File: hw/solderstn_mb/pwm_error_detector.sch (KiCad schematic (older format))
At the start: 14 parts, among them Q1601 DMG1013T, U1601 NE556d, U1602 74LVC1G175dck, U1603 74LVC1G11dck

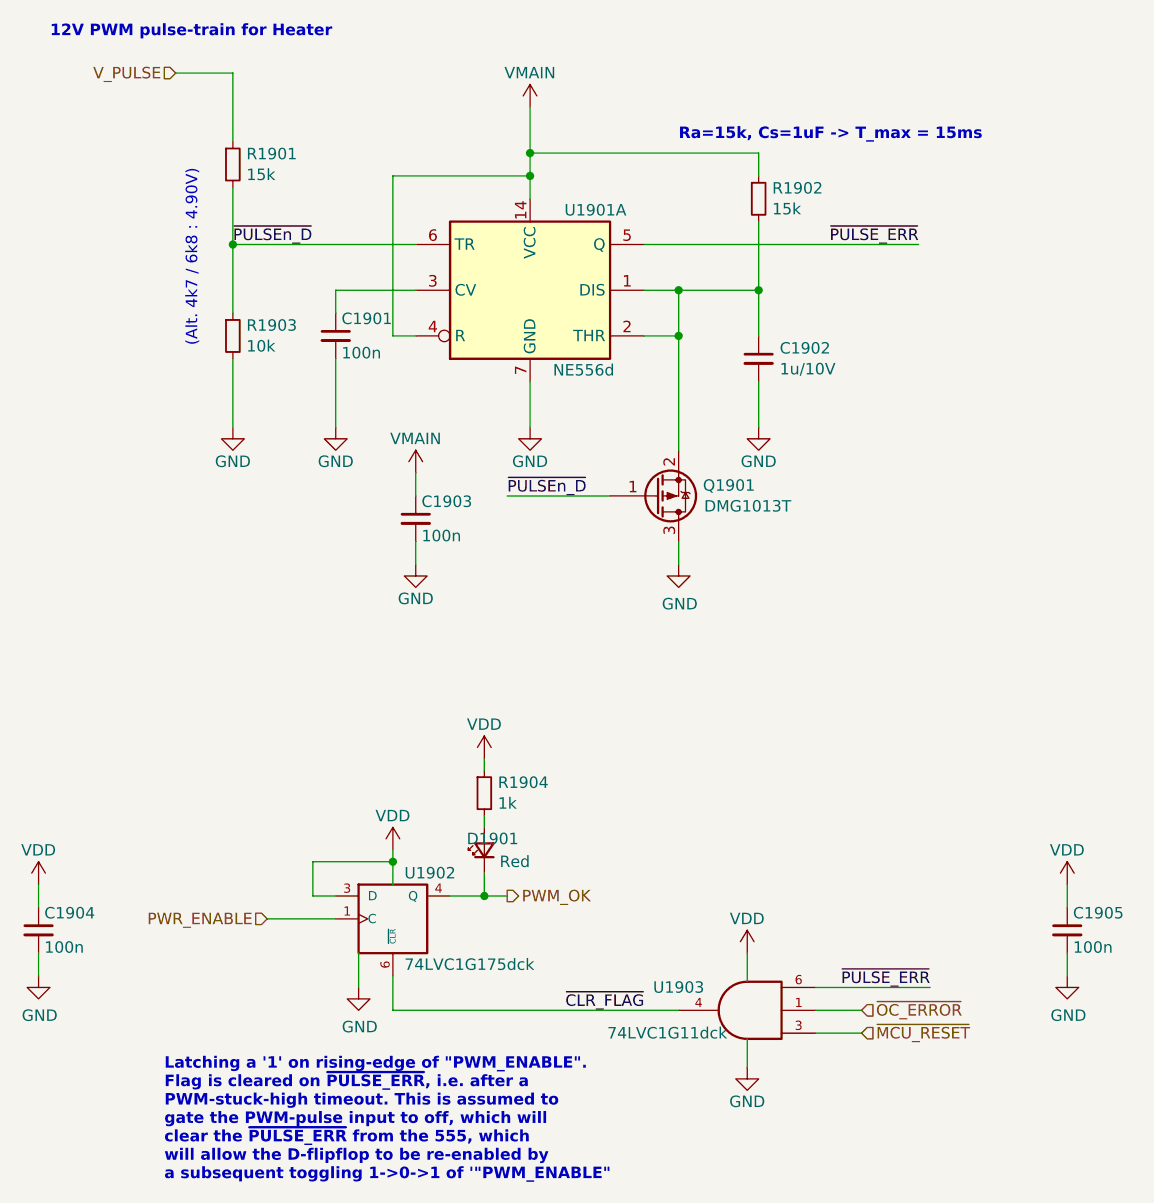
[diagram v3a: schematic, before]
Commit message: Pinout changes to add DS3231 RTC module instead of 32kHz LSE xtal (still keep SMD pads as placeholders). Minor ERC fixes. All footprints specified
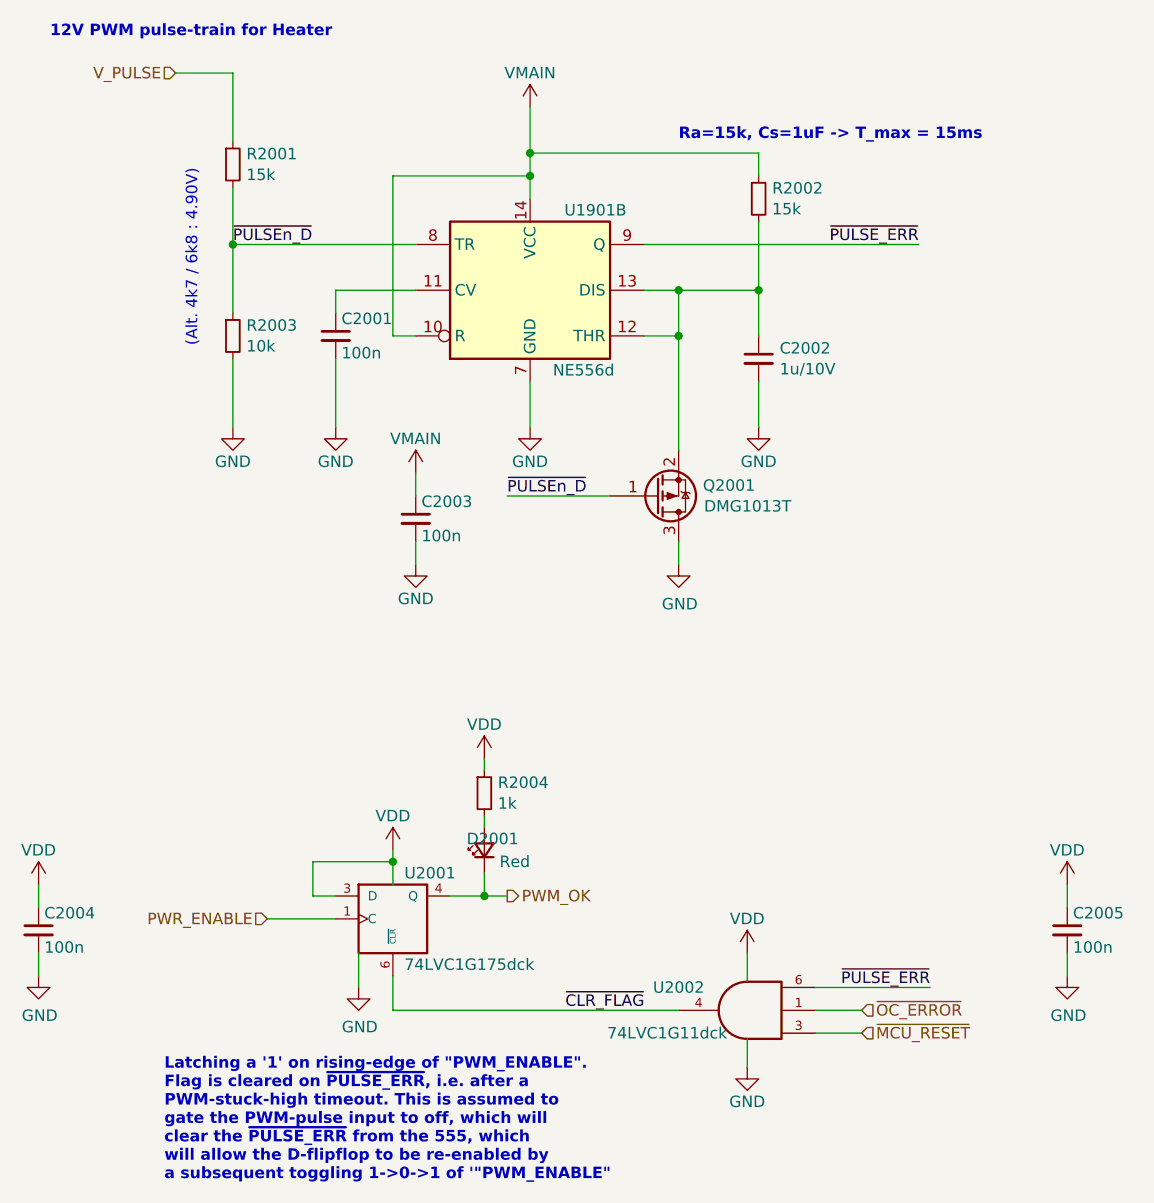
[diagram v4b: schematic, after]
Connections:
- net VMAIN: now also U1601.10 (R); no longer U1601.4 (R)
- net ~PULSE_ERR~: now also U1601.9 (Q); no longer U1601.5 (Q)
- net ~PULSEn_D~: now also U1601.8 (TR); no longer U1601.6 (TR)
- net at C1602.1, Q1601.2 (S), R1602.2: now also U1601.12 (THR), U1601.13 (DIS); no longer U1601.1 (DIS), U1601.2 (THR)
- net at C1601.1: now also U1601.11 (CV); no longer U1601.3 (CV)
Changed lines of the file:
@@
 $Comp
 L Timer:NE556 U1601
-U 1 1 5F5A84E5
+U 2 1 5F5A84E5
 P 4400 2800
 AR Path="/5F785D6E/5F788693/5F5A79BB/5F5A84E5" Ref="U1601"  Part="1"
@@
 F 2 "Package_SO:SOIC-14_3.9x8.7mm_P1.27mm" H 4400 2800 50  0001 C CNN
 F 3 "http://www.ti.com/lit/ds/symlink/ne556.pdf" H 4400 2800 50  0001 C CNN
-	1    4400 2800
+	2    4400 2800
 	1    0    0    -1
 $EndComp
@@
 AR Path="/5F785D6E/5F788A8E/5F5A79BB/5F5A959F" Ref="#PWR01901"  Part="1"
 AR Path="/5F785D6E/5F788A8E/5F5A8042/5F5A959F" Ref="#PWR02001"  Part="1"
-F 0 "#PWR01901" H 4400 1850 50  0001 C CNN
+F 0 "#PWR02001" H 4400 1850 50  0001 C CNN
 F 1 "VMAIN" H 4400 2150 50  0000 C CNN
 F 2 "" H 4400 2000 50  0001 C CNN
@@
 AR Path="/5F785D6E/5F788A8E/5F5A79BB/5F5AA304" Ref="#PWR01904"  Part="1"
 AR Path="/5F785D6E/5F788A8E/5F5A8042/5F5AA304" Ref="#PWR02004"  Part="1"
-F 0 "#PWR01904" H 4400 3150 50  0001 C CNN
+F 0 "#PWR02004" H 4400 3150 50  0001 C CNN
 F 1 "GND" H 4400 3250 50  0000 C CNN
 F 2 "" H 4400 3400 50  0001 C CNN
@@
 AR Path="/5F785D6E/5F788A8E/5F5A79BB/5F5AB1AD" Ref="R1903"  Part="1"
 AR Path="/5F785D6E/5F788A8E/5F5A8042/5F5AB1AD" Ref="R2003"  Part="1"
-F 0 "R1903" H 3159 3046 50  0000 L CNN
+F 0 "R2003" H 3159 3046 50  0000 L CNN
 F 1 "10k" H 3159 2955 50  0000 L CNN
 F 2 "Resistor_SMD:R_0603_1608Metric" H 3100 3000 50  0001 C CNN
@@
 AR Path="/5F785D6E/5F788A8E/5F5A79BB/5F5AB671" Ref="Q1901"  Part="1"
 AR Path="/5F785D6E/5F788A8E/5F5A8042/5F5AB671" Ref="Q2001"  Part="1"
-F 0 "Q1901" H 5156 3654 50  0000 L CNN
+F 0 "Q2001" H 5156 3654 50  0000 L CNN
 F 1 "DMG1013T" H 5352 3745 50  0000 C CNN
 F 2 "customlib_mj_fp:SOT-523" H 5150 3800 50  0001 C CNN
@@
 AR Path="/5F785D6E/5F788A8E/5F5A79BB/5F5ABF55" Ref="#PWR01908"  Part="1"
 AR Path="/5F785D6E/5F788A8E/5F5A8042/5F5ABF55" Ref="#PWR02008"  Part="1"
-F 0 "#PWR01908" H 5050 3750 50  0001 C CNN
+F 0 "#PWR02008" H 5050 3750 50  0001 C CNN
 F 1 "GND" H 5055 3827 50  0000 C CNN
 F 2 "" H 5050 4000 50  0001 C CNN
@@
 AR Path="/5F785D6E/5F788A8E/5F5A79BB/5F5AD420" Ref="C1901"  Part="1"
 AR Path="/5F785D6E/5F788A8E/5F5A8042/5F5AD420" Ref="C2001"  Part="1"
-F 0 "C1901" H 3575 3075 50  0000 L CNN
+F 0 "C2001" H 3575 3075 50  0000 L CNN
 F 1 "100n" H 3575 2925 50  0000 L CNN
 F 2 "Capacitor_SMD:C_0603_1608Metric" H 3550 3000 50  0001 C CNN
@@
 AR Path="/5F785D6E/5F788A8E/5F5A79BB/5F5AE7F1" Ref="#PWR01903"  Part="1"
 AR Path="/5F785D6E/5F788A8E/5F5A8042/5F5AE7F1" Ref="#PWR02003"  Part="1"
-F 0 "#PWR01903" H 3550 3150 50  0001 C CNN
+F 0 "#PWR02003" H 3550 3150 50  0001 C CNN
 F 1 "GND" H 3550 3250 50  0000 C CNN
 F 2 "" H 3550 3400 50  0001 C CNN
@@
 AR Path="/5F785D6E/5F788A8E/5F5A79BB/5F5B187D" Ref="#PWR01905"  Part="1"
 AR Path="/5F785D6E/5F788A8E/5F5A8042/5F5B187D" Ref="#PWR02005"  Part="1"
-F 0 "#PWR01905" H 5400 3150 50  0001 C CNN
+F 0 "#PWR02005" H 5400 3150 50  0001 C CNN
 F 1 "GND" H 5400 3250 50  0000 C CNN
 F 2 "" H 5400 3400 50  0001 C CNN
@@
 AR Path="/5F785D6E/5F788A8E/5F5A79BB/5F5AABE9" Ref="C1902"  Part="1"
 AR Path="/5F785D6E/5F788A8E/5F5A8042/5F5AABE9" Ref="C2002"  Part="1"
-F 0 "C1902" H 5492 3146 50  0000 L CNN
+F 0 "C2002" H 5492 3146 50  0000 L CNN
 F 1 "1u/10V" H 5492 3055 50  0000 L CNN
 F 2 "Capacitor_SMD:C_0603_1608Metric" H 5400 3100 50  0001 C CNN
@@
 AR Path="/5F785D6E/5F788A8E/5F5A79BB/5F5B2A12" Ref="R1902"  Part="1"
 AR Path="/5F785D6E/5F788A8E/5F5A8042/5F5B2A12" Ref="R2002"  Part="1"
-F 0 "R1902" H 5459 2446 50  0000 L CNN
+F 0 "R2002" H 5459 2446 50  0000 L CNN
 F 1 "15k" H 5459 2355 50  0000 L CNN
 F 2 "Resistor_SMD:R_0603_1608Metric" H 5400 2400 50  0001 C CNN
@@
 AR Path="/5F785D6E/5F788A8E/5F5A79BB/5F5B486D" Ref="R1901"  Part="1"
 AR Path="/5F785D6E/5F788A8E/5F5A8042/5F5B486D" Ref="R2001"  Part="1"
-F 0 "R1901" H 3159 2296 50  0000 L CNN
+F 0 "R2001" H 3159 2296 50  0000 L CNN
 F 1 "15k" H 3159 2205 50  0000 L CNN
 F 2 "Resistor_SMD:R_0603_1608Metric" H 3100 2250 50  0001 C CNN
@@
 AR Path="/5F785D6E/5F788A8E/5F5A79BB/5F5B6E87" Ref="#PWR01902"  Part="1"
 AR Path="/5F785D6E/5F788A8E/5F5A8042/5F5B6E87" Ref="#PWR02002"  Part="1"
-F 0 "#PWR01902" H 3100 3150 50  0001 C CNN
+F 0 "#PWR02002" H 3100 3150 50  0001 C CNN
 F 1 "GND" H 3100 3250 50  0000 C CNN
 F 2 "" H 3100 3400 50  0001 C CNN
@@
 AR Path="/5F785D6E/5F788A8E/5F5A79BB/5F5BA510" Ref="#PWR01906"  Part="1"
 AR Path="/5F785D6E/5F788A8E/5F5A8042/5F5BA510" Ref="#PWR02006"  Part="1"
-F 0 "#PWR01906" H 3900 3450 50  0001 C CNN
+F 0 "#PWR02006" H 3900 3450 50  0001 C CNN
 F 1 "VMAIN" H 3900 3750 50  0000 C CNN
 F 2 "" H 3900 3600 50  0001 C CNN
@@
 AR Path="/5F785D6E/5F788A8E/5F5A79BB/5F5BB79F" Ref="#PWR01907"  Part="1"
 AR Path="/5F785D6E/5F788A8E/5F5A8042/5F5BB79F" Ref="#PWR02007"  Part="1"
-F 0 "#PWR01907" H 3900 3750 50  0001 C CNN
+F 0 "#PWR02007" H 3900 3750 50  0001 C CNN
 F 1 "GND" H 3900 3850 50  0000 C CNN
 F 2 "" H 3900 4000 50  0001 C CNN
@@
 AR Path="/5F785D6E/5F788A8E/5F5A79BB/5F5BB9DE" Ref="C1903"  Part="1"
 AR Path="/5F785D6E/5F788A8E/5F5A8042/5F5BB9DE" Ref="C2003"  Part="1"
-F 0 "C1903" H 3925 3875 50  0000 L CNN
+F 0 "C2003" H 3925 3875 50  0000 L CNN
 F 1 "100n" H 3925 3725 50  0000 L CNN
 F 2 "Capacitor_SMD:C_0603_1608Metric" H 3900 3800 50  0001 C CNN
@@
 AR Path="/5F785D6E/5F788A8E/5F5A79BB/5F5C5CBD" Ref="U1902"  Part="1"
 AR Path="/5F785D6E/5F788A8E/5F5A8042/5F5C5CBD" Ref="U2001"  Part="1"
-F 0 "U1902" H 3850 5750 50  0000 L CNN
+F 0 "U2001" H 3850 5750 50  0000 L CNN
 F 1 "74LVC1G175dck" H 3850 5350 50  0000 L CNN
 F 2 "Package_TO_SOT_SMD:SOT-363_SC-70-6_Handsoldering" H 3800 5550 50  0001 C CNN
@@
 AR Path="/5F785D6E/5F788A8E/5F5A79BB/5F5C6FB1" Ref="#PWR01910"  Part="1"
 AR Path="/5F785D6E/5F788A8E/5F5A8042/5F5C6FB1" Ref="#PWR02010"  Part="1"
-F 0 "#PWR01910" H 3800 5100 50  0001 C CNN
+F 0 "#PWR02010" H 3800 5100 50  0001 C CNN
 F 1 "VDD" H 3800 5400 50  0000 C CNN
 F 2 "" H 3800 5250 50  0001 C CNN
@@
 AR Path="/5F785D6E/5F788A8E/5F5A79BB/5F5C7E80" Ref="#PWR01916"  Part="1"
 AR Path="/5F785D6E/5F788A8E/5F5A8042/5F5C7E80" Ref="#PWR02016"  Part="1"
-F 0 "#PWR01916" H 3650 5600 50  0001 C CNN
+F 0 "#PWR02016" H 3650 5600 50  0001 C CNN
 F 1 "GND" H 3655 5677 50  0000 C CNN
 F 2 "" H 3650 5850 50  0001 C CNN
@@
 AR Path="/5F785D6E/5F788A8E/5F5A79BB/5F5C95DA" Ref="#PWR01911"  Part="1"
 AR Path="/5F785D6E/5F788A8E/5F5A8042/5F5C95DA" Ref="#PWR02011"  Part="1"
-F 0 "#PWR01911" H 2250 5250 50  0001 C CNN
+F 0 "#PWR02011" H 2250 5250 50  0001 C CNN
 F 1 "VDD" H 2250 5550 50  0000 C CNN
 F 2 "" H 2250 5400 50  0001 C CNN
@@
 AR Path="/5F785D6E/5F788A8E/5F5A79BB/5F5C9F45" Ref="#PWR01914"  Part="1"
 AR Path="/5F785D6E/5F788A8E/5F5A8042/5F5C9F45" Ref="#PWR02014"  Part="1"
-F 0 "#PWR01914" H 2250 5550 50  0001 C CNN
+F 0 "#PWR02014" H 2250 5550 50  0001 C CNN
 F 1 "GND" H 2255 5627 50  0000 C CNN
 F 2 "" H 2250 5800 50  0001 C CNN
@@
 AR Path="/5F785D6E/5F788A8E/5F5A79BB/5F5CA18F" Ref="C1904"  Part="1"
 AR Path="/5F785D6E/5F788A8E/5F5A8042/5F5CA18F" Ref="C2004"  Part="1"
-F 0 "C1904" H 2275 5675 50  0000 L CNN
+F 0 "C2004" H 2275 5675 50  0000 L CNN
 F 1 "100n" H 2275 5525 50  0000 L CNN
 F 2 "Capacitor_SMD:C_0603_1608Metric" H 2250 5600 50  0001 C CNN
@@
 AR Path="/5F785D6E/5F788A8E/5F5A79BB/5F5D2DC0" Ref="R1904"  Part="1"
 AR Path="/5F785D6E/5F788A8E/5F5A8042/5F5D2DC0" Ref="R2004"  Part="1"
-F 0 "R1904" H 4259 5046 50  0000 L CNN
+F 0 "R2004" H 4259 5046 50  0000 L CNN
 F 1 "1k" H 4259 4955 50  0000 L CNN
 F 2 "Resistor_SMD:R_0603_1608Metric" H 4200 5000 50  0001 C CNN
@@
 AR Path="/5F785D6E/5F788A8E/5F5A79BB/5F5D37AB" Ref="D1901"  Part="1"
 AR Path="/5F785D6E/5F788A8E/5F5A8042/5F5D37AB" Ref="D2001"  Part="1"
-F 0 "D1901" V 4250 5100 50  0000 L CNN
+F 0 "D2001" V 4250 5100 50  0000 L CNN
 F 1 "Red" V 4150 5050 50  0000 L CNN
 F 2 "LED_SMD:LED_0603_1608Metric" V 4200 5250 50  0001 C CNN
@@
 AR Path="/5F785D6E/5F788A8E/5F5A79BB/5F5D912D" Ref="#PWR01909"  Part="1"
 AR Path="/5F785D6E/5F788A8E/5F5A8042/5F5D912D" Ref="#PWR02009"  Part="1"
-F 0 "#PWR01909" H 4200 4700 50  0001 C CNN
+F 0 "#PWR02009" H 4200 4700 50  0001 C CNN
 F 1 "VDD" H 4200 5000 50  0000 C CNN
 F 2 "" H 4200 4850 50  0001 C CNN
@@
 AR Path="/5F785D6E/5F788A8E/5F5A79BB/5F774422" Ref="U1903"  Part="1"
 AR Path="/5F785D6E/5F788A8E/5F5A8042/5F774422" Ref="U2002"  Part="1"
-F 0 "U1903" H 5650 6050 50  0000 C CNN
+F 0 "U2002" H 5650 6050 50  0000 C CNN
 F 1 "74LVC1G11dck" H 5700 5850 50  0000 C CNN
 F 2 "Package_TO_SOT_SMD:SOT-363_SC-70-6_Handsoldering" H 5350 5950 50  0001 C CNN
@@
 AR Path="/5F785D6E/5F788A8E/5F5A79BB/5F775144" Ref="#PWR01913"  Part="1"
 AR Path="/5F785D6E/5F788A8E/5F5A8042/5F775144" Ref="#PWR02013"  Part="1"
-F 0 "#PWR01913" H 5350 5550 50  0001 C CNN
+F 0 "#PWR02013" H 5350 5550 50  0001 C CNN
 F 1 "VDD" H 5350 5850 50  0000 C CNN
 F 2 "" H 5350 5700 50  0001 C CNN
@@
 AR Path="/5F785D6E/5F788A8E/5F5A79BB/5F776769" Ref="#PWR01917"  Part="1"
 AR Path="/5F785D6E/5F788A8E/5F5A8042/5F776769" Ref="#PWR02017"  Part="1"
-F 0 "#PWR01917" H 5350 5950 50  0001 C CNN
+F 0 "#PWR02017" H 5350 5950 50  0001 C CNN
 F 1 "GND" H 5350 6050 50  0000 C CNN
 F 2 "" H 5350 6200 50  0001 C CNN
@@
 AR Path="/5F785D6E/5F788A8E/5F5A79BB/5F78BCE9" Ref="#PWR01912"  Part="1"
 AR Path="/5F785D6E/5F788A8E/5F5A8042/5F78BCE9" Ref="#PWR02012"  Part="1"
-F 0 "#PWR01912" H 6750 5250 50  0001 C CNN
+F 0 "#PWR02012" H 6750 5250 50  0001 C CNN
 F 1 "VDD" H 6750 5550 50  0000 C CNN
 F 2 "" H 6750 5400 50  0001 C CNN
@@
 AR Path="/5F785D6E/5F788A8E/5F5A79BB/5F78BCF3" Ref="#PWR01915"  Part="1"
 AR Path="/5F785D6E/5F788A8E/5F5A8042/5F78BCF3" Ref="#PWR02015"  Part="1"
-F 0 "#PWR01915" H 6750 5550 50  0001 C CNN
+F 0 "#PWR02015" H 6750 5550 50  0001 C CNN
 F 1 "GND" H 6755 5627 50  0000 C CNN
 F 2 "" H 6750 5800 50  0001 C CNN
@@
 AR Path="/5F785D6E/5F788A8E/5F5A79BB/5F78BCFD" Ref="C1905"  Part="1"
 AR Path="/5F785D6E/5F788A8E/5F5A8042/5F78BCFD" Ref="C2005"  Part="1"
-F 0 "C1905" H 6775 5675 50  0000 L CNN
+F 0 "C2005" H 6775 5675 50  0000 L CNN
 F 1 "100n" H 6775 5525 50  0000 L CNN
 F 2 "Capacitor_SMD:C_0603_1608Metric" H 6750 5600 50  0001 C CNN
